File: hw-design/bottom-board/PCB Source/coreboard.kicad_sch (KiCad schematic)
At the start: 30 parts, among them J2 Conn_01x25, J3 AS0A823-H4SB-7H, J6 SERIAL_DEBUG, U7 AT24CS08

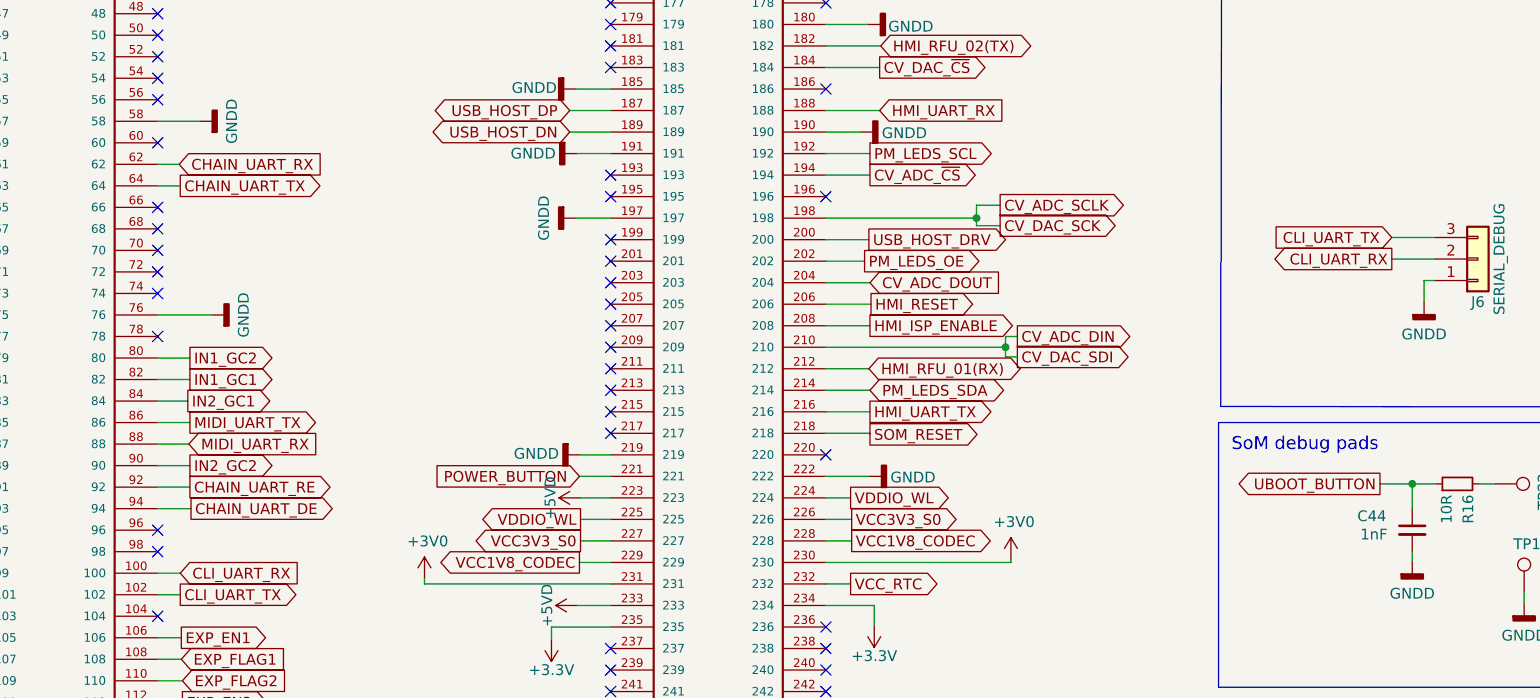
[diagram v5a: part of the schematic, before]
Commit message: mainboard: correct CC TX pin + update fabrication files
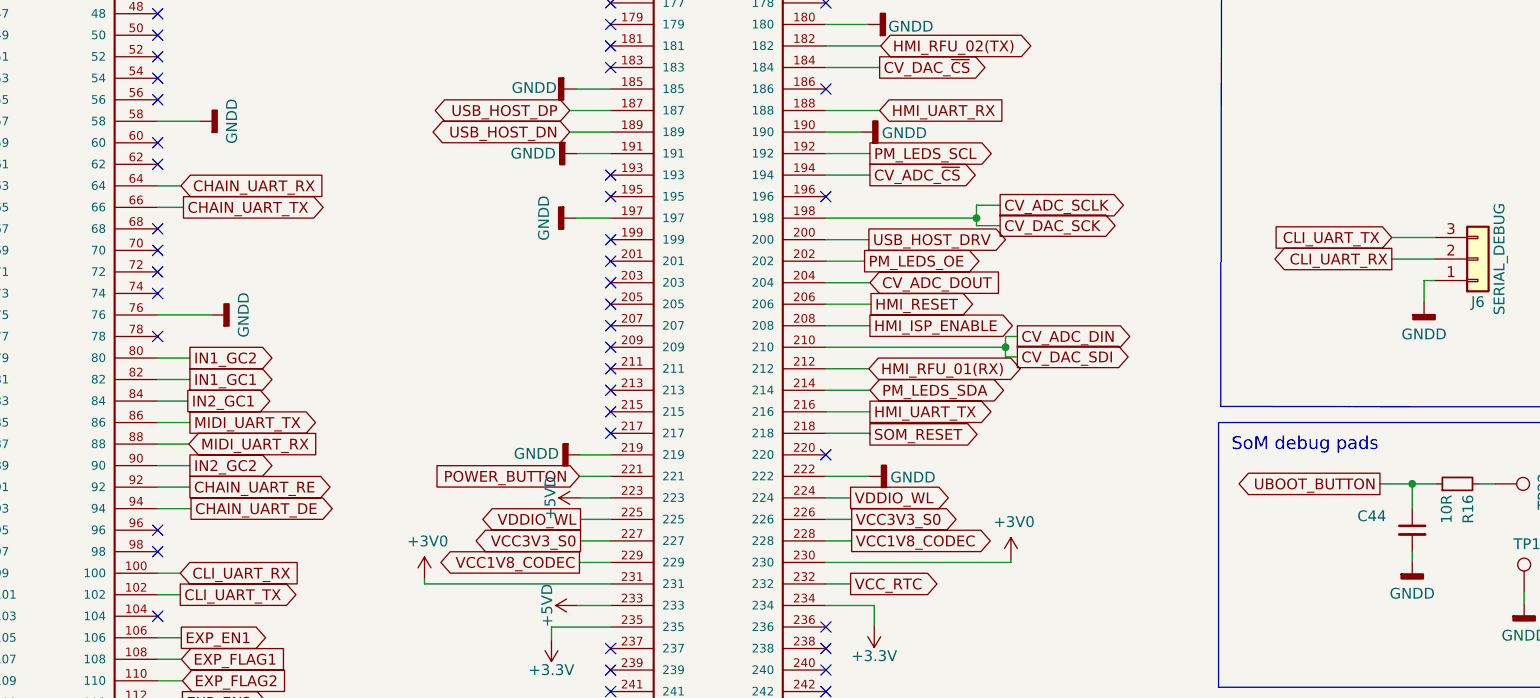
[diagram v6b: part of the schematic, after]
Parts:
- C44: value 1nF -> (none); footprint Capacitor_SMD:C_0603_1608Metric -> (none); MPN C0603X7R500-103KNP -> C0603X7R500-102KNP
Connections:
- net CHAIN_UART_RX: now also J3.64; no longer J3.62
- net CHAIN_UART_TX: now also J3.66; no longer J3.64
